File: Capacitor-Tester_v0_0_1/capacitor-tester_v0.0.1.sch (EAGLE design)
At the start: 6 parts, among them U1 AD5933, Y1 LFSPXO018034

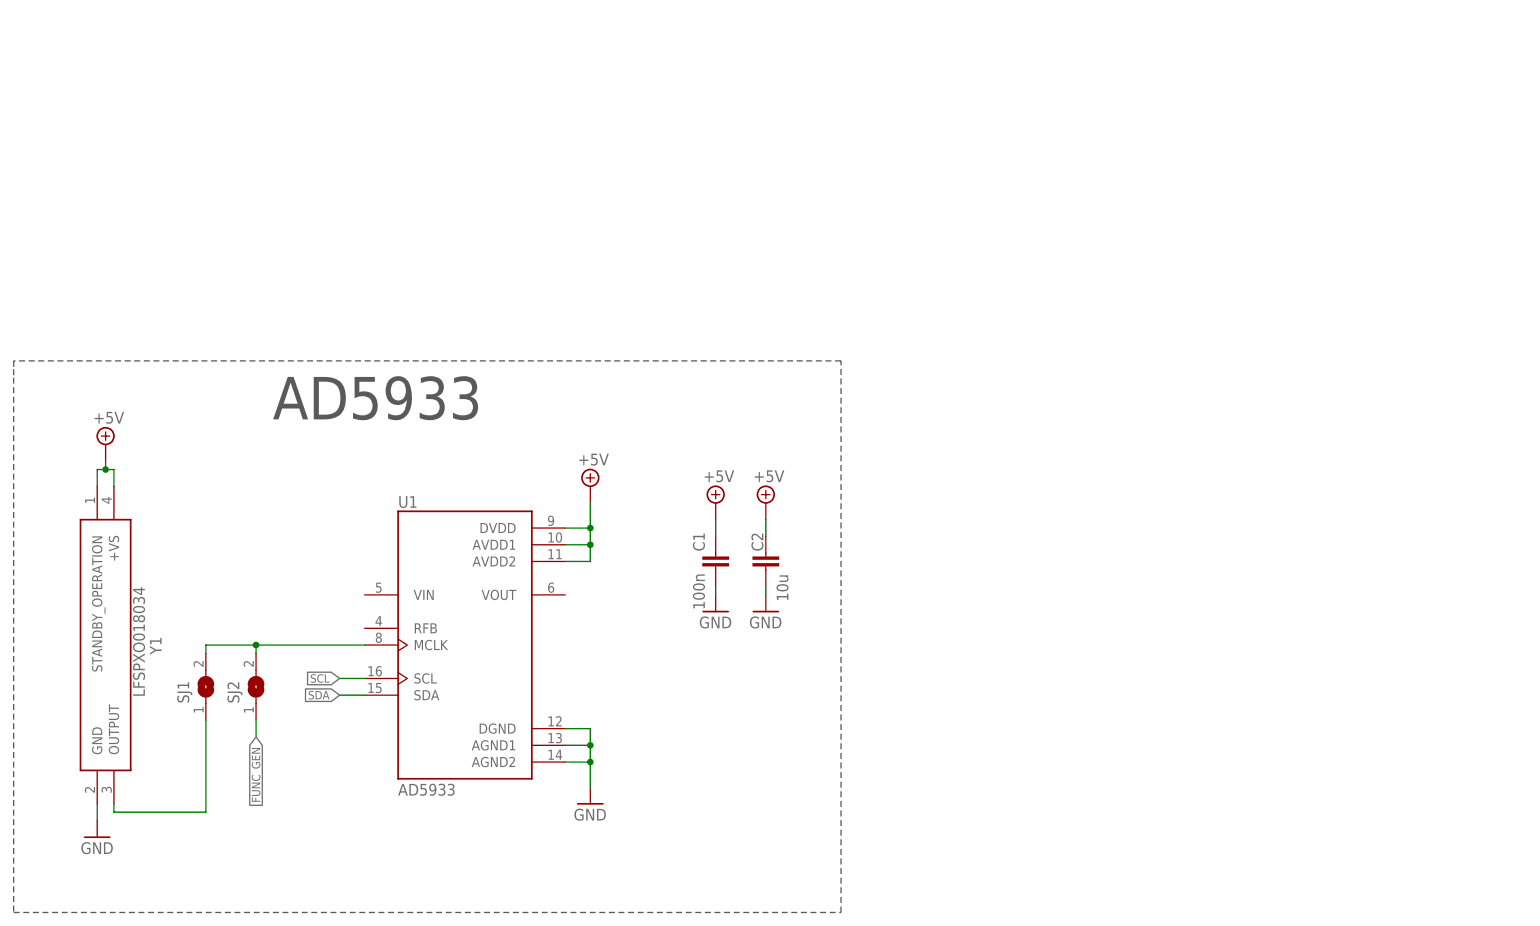
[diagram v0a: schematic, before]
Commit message: v0.0.1 - Finished the first stage of AD5933 opamp and added usb c connector for the power supply
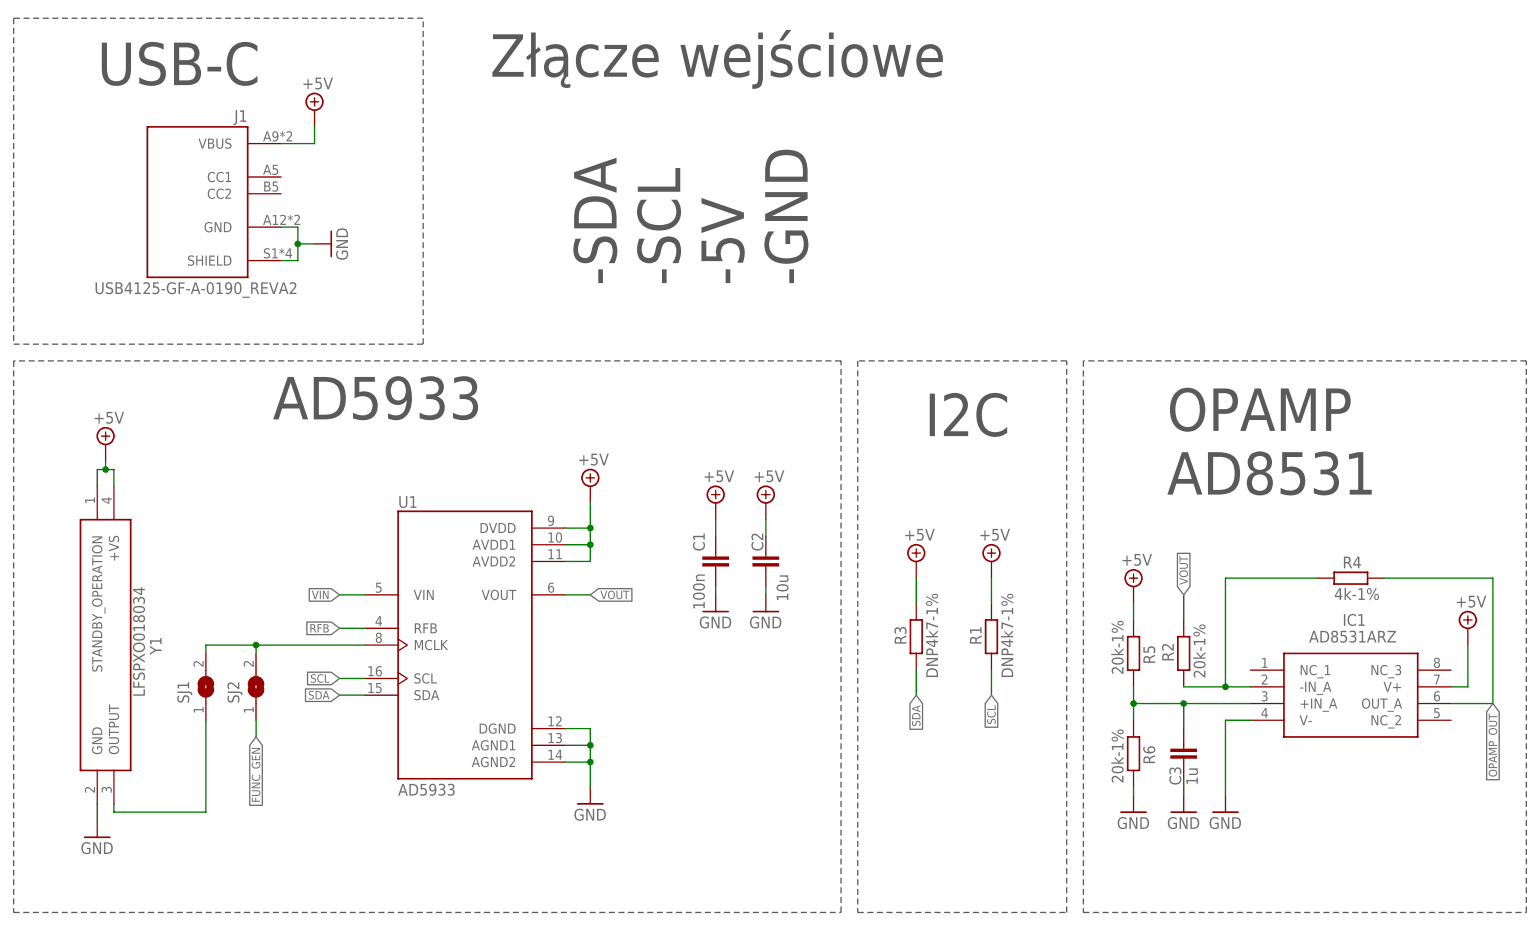
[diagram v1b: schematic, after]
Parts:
- added C3: 1u, custom_library:CAPACITOR_SMD_CERAMIC0603
- added IC1: AD8531ARZ, AD8531ARZ:AD8531ARZ
- added J1: USB4125-GF-A-0190_REVA2, USB-C-6Pin:USB4125-GF-A-0190_REVA2
- added R1, R3: DNP4k7-1%, custom_library:RESISTOR_SMD0603
- added R2, R5, R6: 20k-1%, custom_library:RESISTOR_SMD0603
- added R4: 4k-1%, custom_library:RESISTOR_SMD0603
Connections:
- new net N$1: IC1.-IN_A, R2.1, R4.1
- new net N$4: C3.1, IC1.+IN_A, R5.2, R6.1
- new net OPAMP_OUT: IC1.OUT_A, R4.2
- new net RFB: U1.RFB
- new net VIN: U1.VIN
- new net VOUT: R2.2, U1.VOUT
- net +5V: now also IC1.V+, J1.VBUS, R1.2, R3.2, R5.1
- net GND: now also C3.2, IC1.V-, J1.GND, J1.SHIELD, R6.2
- net SCL: now also R1.1
- net SDA: now also R3.1
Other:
- note added: "-SDA -SCL -5V -GND"
- note added: "I2C"
- note added: "OPAMP AD8531"
- note added: "USB-C"
- note added: "Złącze wejściowe"

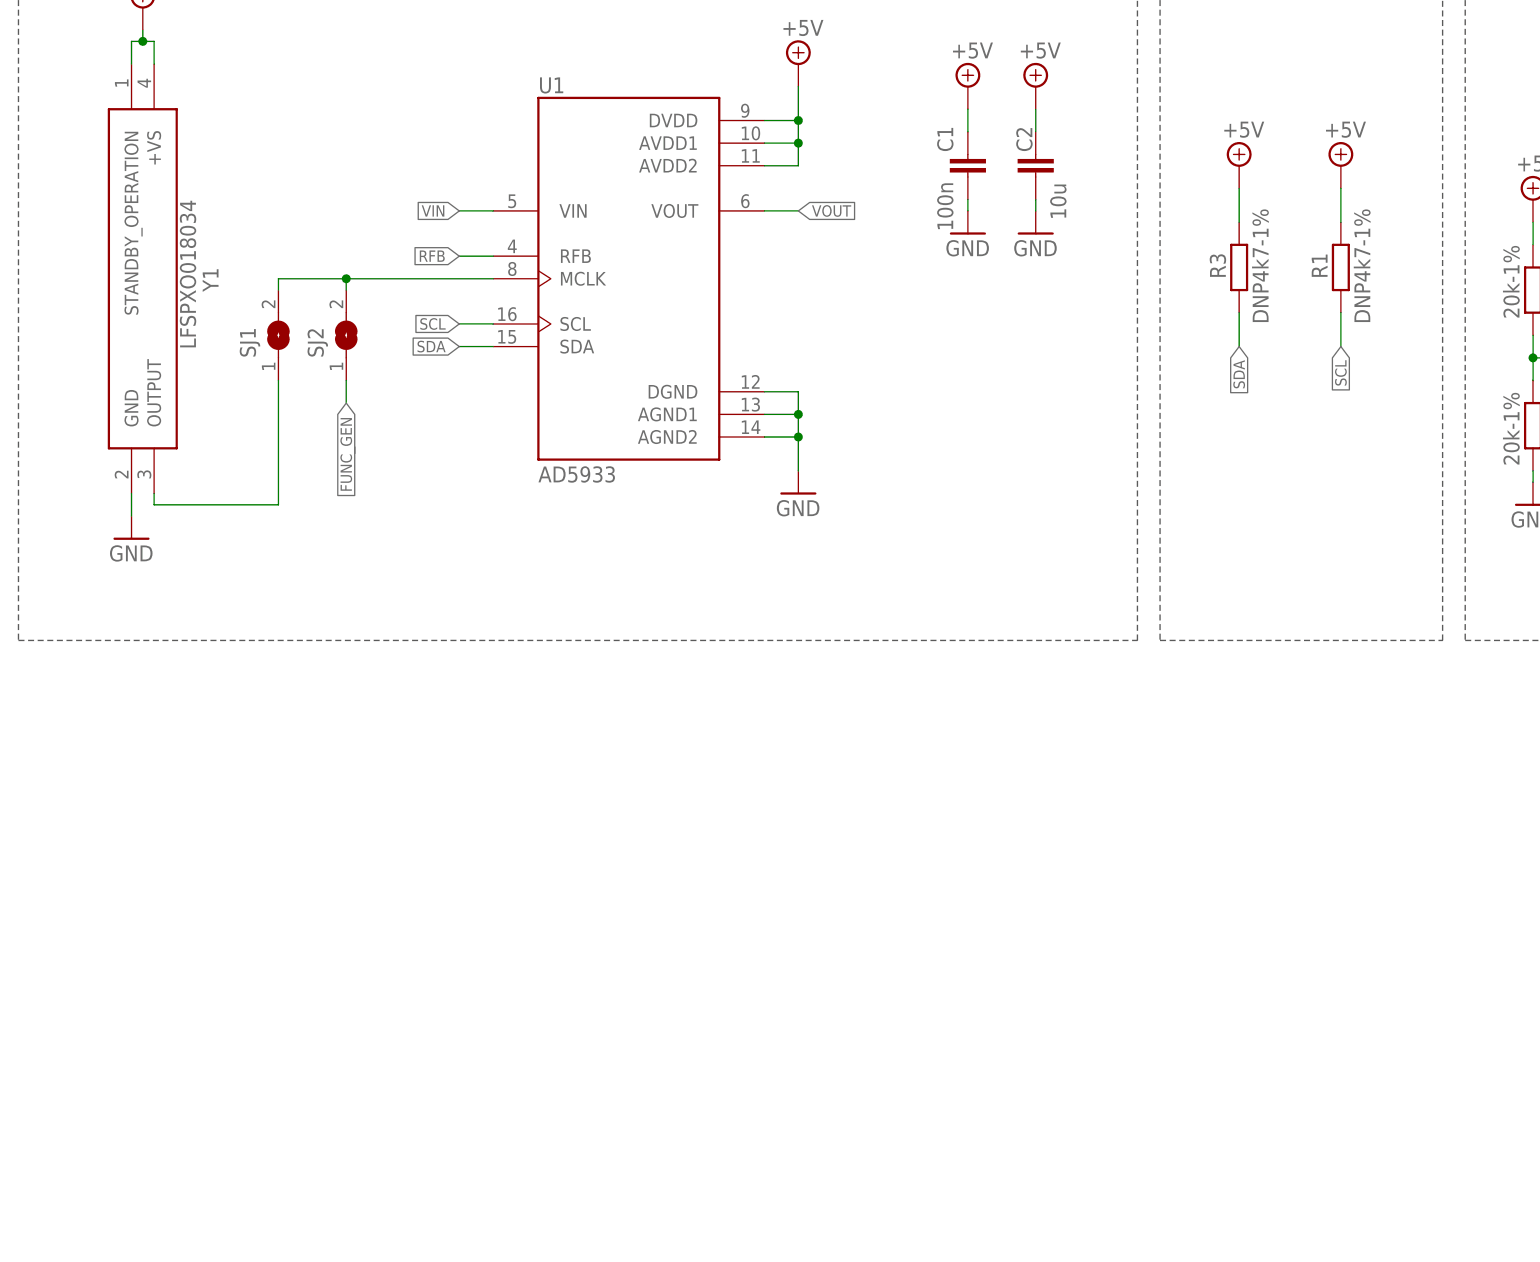
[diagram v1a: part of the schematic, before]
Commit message: v0.0.1 - Added two stages of the opamps. Need to add boost converter for the second opamp
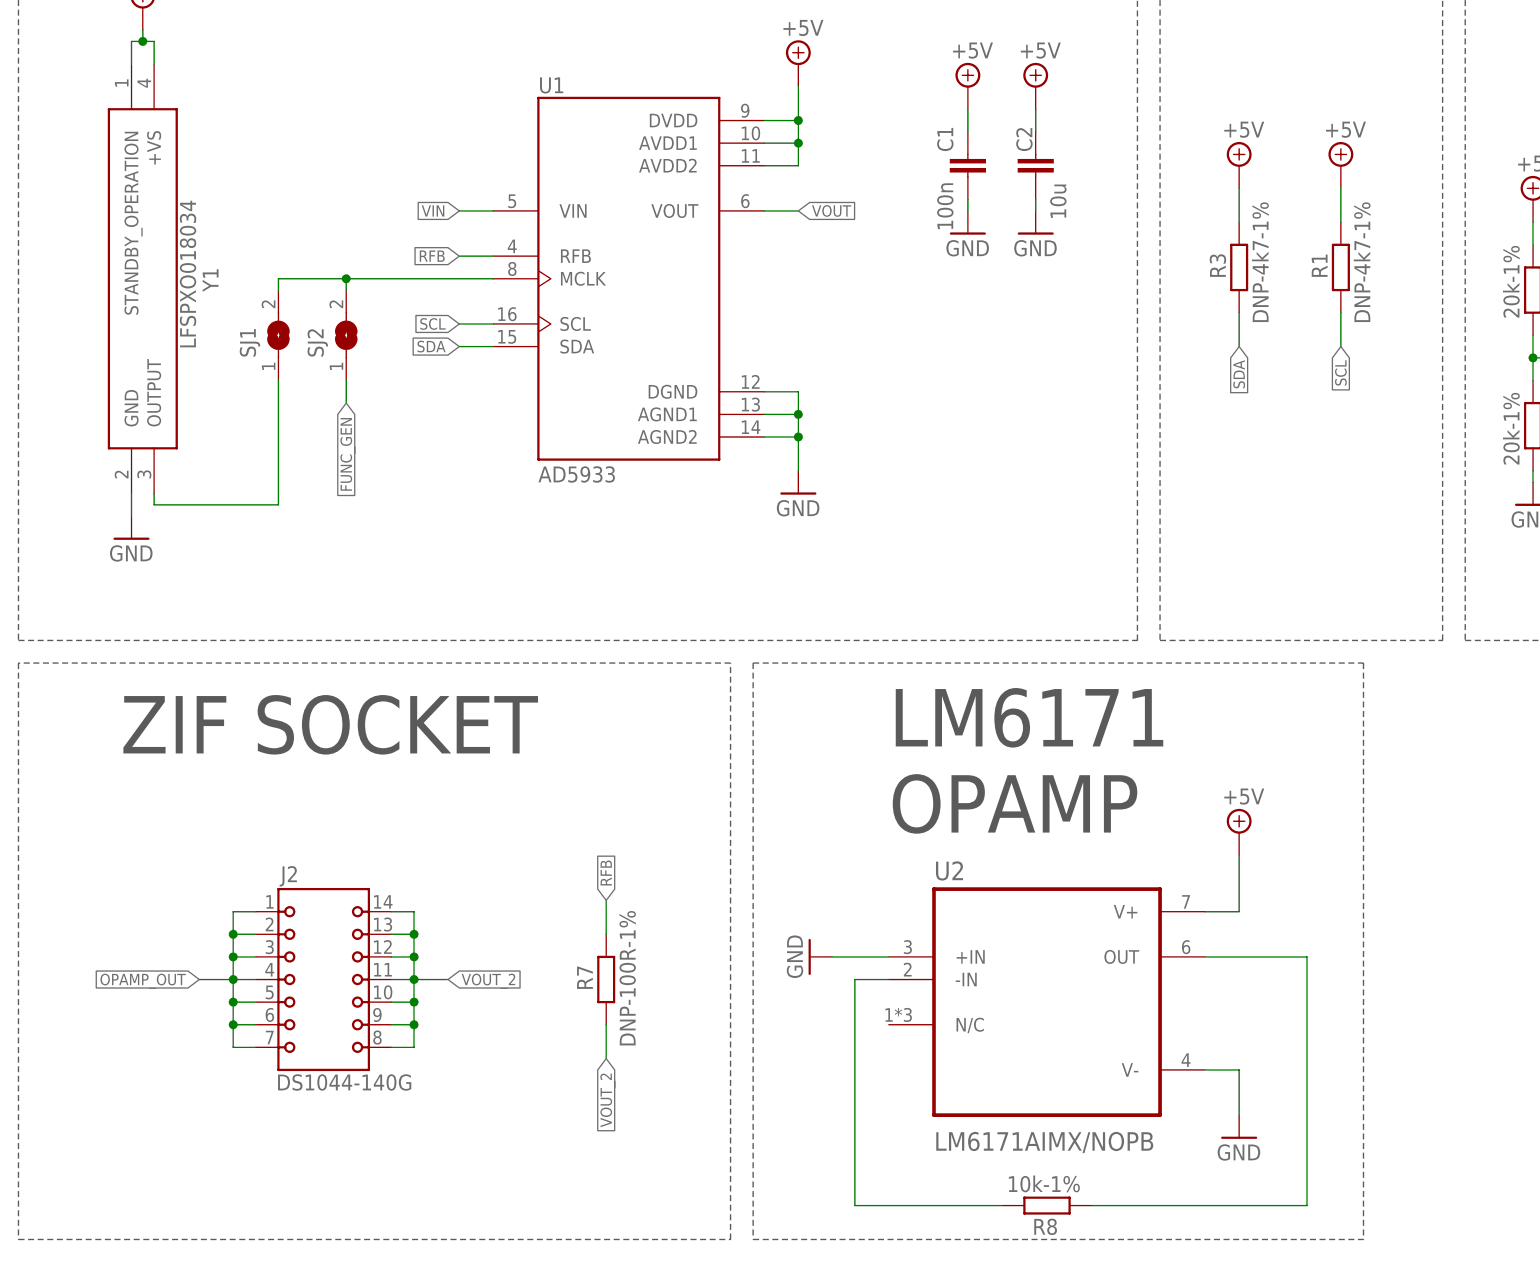
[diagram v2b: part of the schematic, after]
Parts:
- added J2: DS1044-140G, DS1044-140G:DS1044-140G
- added R7: DNP-100R-1%, custom_library:RESISTOR_SMD0603
- added R8: 10k-1%, custom_library:RESISTOR_SMD0603
- added U2: LM6171AIMX/NOPB, LM6171AIMX_NOPB:LM6171AIMX/NOPB
- R1, R3: value DNP4k7-1% -> DNP-4k7-1%
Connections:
- new net N$2: R8.2, U2.-IN
- new net N$3: R8.1, U2.OUT
- new net VOUT_2: J2.10, J2.11, J2.12, J2.13, J2.14, J2.8, J2.9, R7.1
- net +5V: now also U2.V+
- net GND: now also U2.+IN, U2.V-
- net OPAMP_OUT: now also J2.1, J2.2, J2.3, J2.4, J2.5, J2.6, J2.7
- net RFB: now also R7.2
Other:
- note added: "LM6171 OPAMP"
- note added: "ZIF SOCKET"
